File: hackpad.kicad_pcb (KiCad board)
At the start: 2 copper layers, 65 x 80 mm, 39 parts, among them J1 Conn_01x04_Socket, SW1 SW_Push_45deg, SW13 RotaryEncoder_Switch, SW2 SW_Push_45deg, SW3 SW_Push_45deg, SW4 SW_Push_45deg, SW5 SW_Push_45deg, SW6 SW_Push_45deg, SW7 SW_Push_45deg, SW8 SW_Push_45deg, U1 XIAO-RP2040-DIP

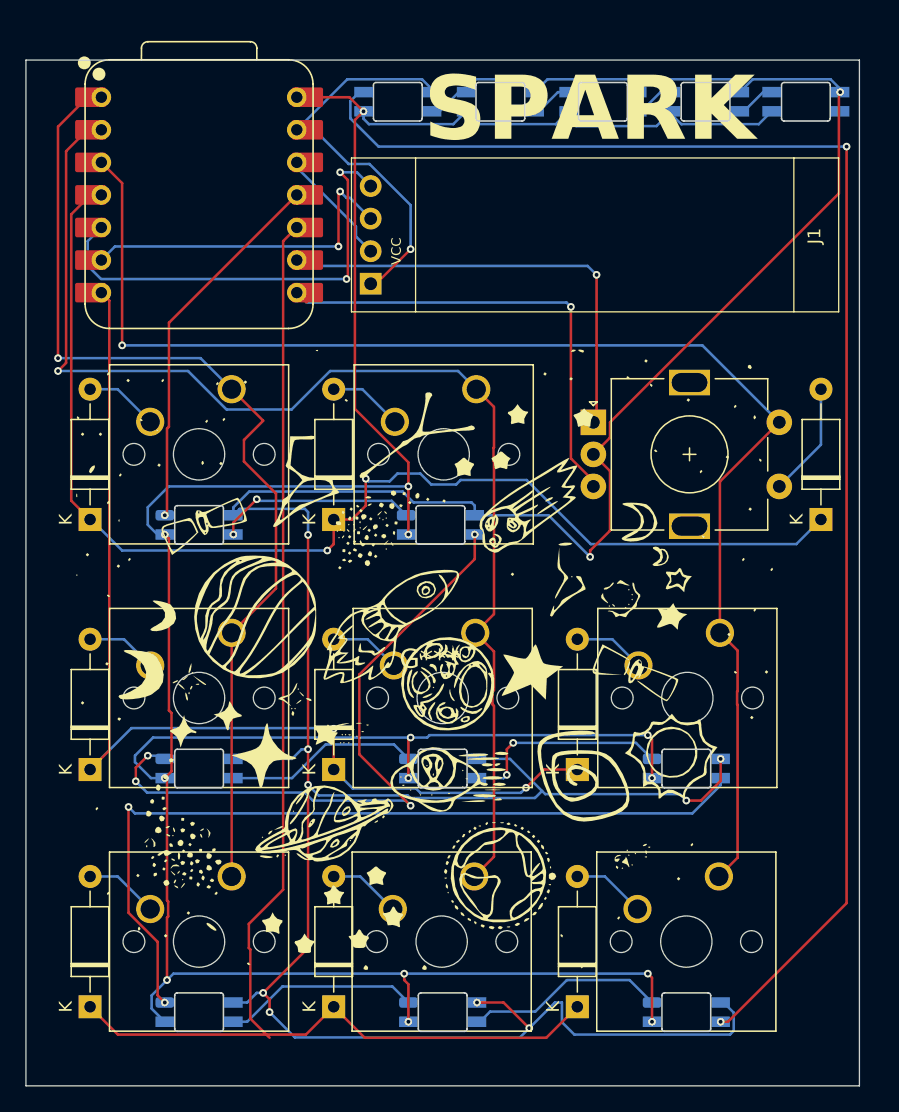
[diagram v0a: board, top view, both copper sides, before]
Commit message: Add GND fill , removed via from pads
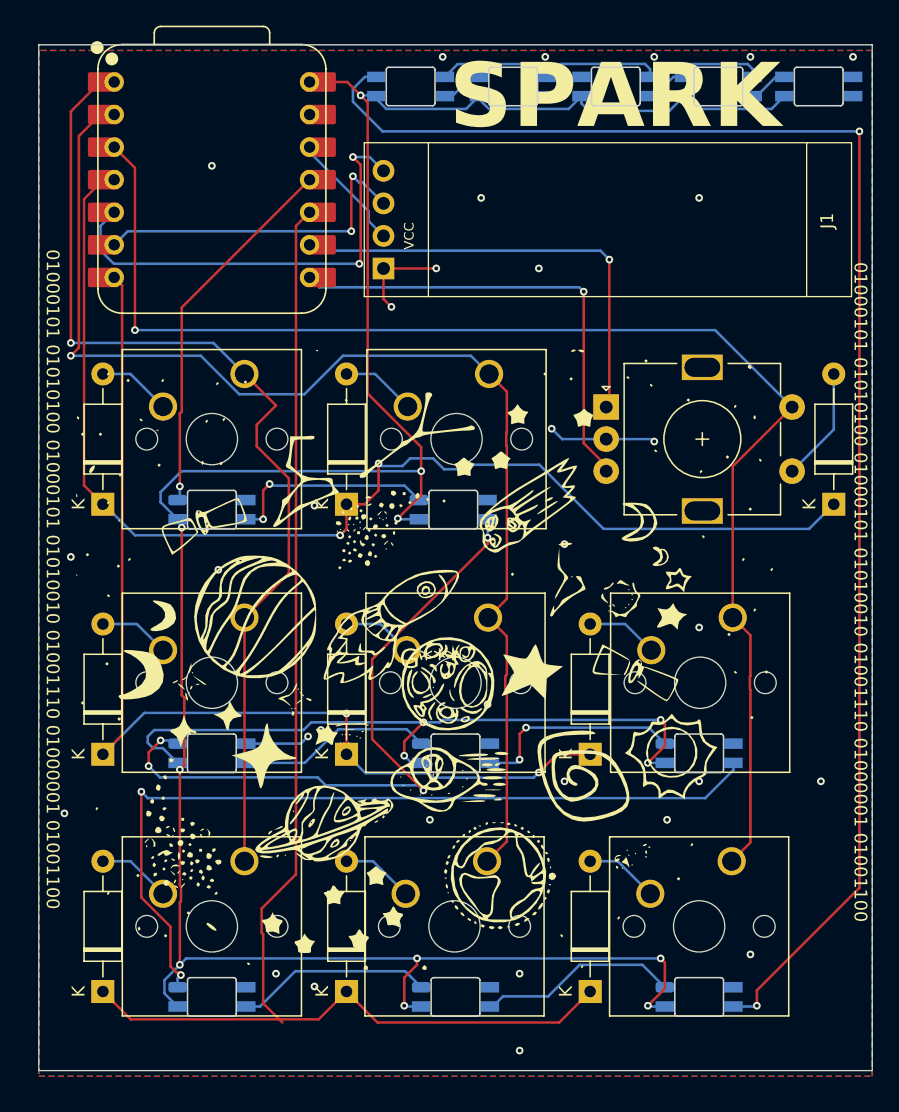
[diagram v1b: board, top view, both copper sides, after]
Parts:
- moved D1 1.55 mm to (106.0, 128.9)
- moved D2 1.55 mm to (125.0, 128.9)
- moved D3 1.55 mm to (106.0, 90.9)
- moved D4 1.55 mm to (125.0, 90.9)
- moved D5 1.55 mm to (163.0, 90.9)
- moved D6 1.55 mm to (106.0, 110.4)
- moved D7 1.55 mm to (125.0, 110.4)
- moved D8 1.55 mm to (144.0, 110.4)
- moved D9 1.55 mm to (144.0, 128.9)
- moved J1 1.55 mm to (164.4, 74.7)
- moved LD1 1.55 mm to (114.5, 91.3)
- moved LD2 1.55 mm to (133.3, 91.3)
- moved LD3 1.55 mm to (114.5, 110.3)
- moved LD4 1.55 mm to (133.5, 110.3)
- moved LD5 1.55 mm to (152.5, 110.3)
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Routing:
- net GND: track 290.3 -> 50.5 mm, vias 13 -> 32
- net VBUS: track 236.6 -> 245.7 mm
- net Net-(LD8-DOUT): track 114.9 -> 117.0 mm
- net Net-(LD1-DOUT): track 15.8 -> 16.6 mm
- added copper zone on B.Cu, net GND
- added copper zone on F.Cu, net GND
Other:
- board text added: "01000101 01010100 01000101 01010010 01001110 01000001 01001100"
